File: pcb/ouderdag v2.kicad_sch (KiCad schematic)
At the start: 18 parts, among them J1 Conn_01x05_Pin, J2 Conn_01x05_Pin, J3 Conn_01x05_Socket, J4 Conn_01x05_Socket, J5 Conn_01x06_Pin, SW1 SW_Push, U1 ATtiny85

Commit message: updated code and pcb
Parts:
- removed C1: C, Capacitor_THT:CP_Radial_D8.0mm_P3.50mm, symbol Device:C
- removed J5: Conn_01x06_Pin, Connector_PinHeader_2.54mm:PinHeader_1x06_P2.54mm_Vertical, symbol Connector:Conn_01x06_Pin
- added J5: Conn_01x03_Socket, Connector_PinSocket_2.54mm:PinSocket_1x03_P2.54mm_Vertical, symbol Connector:Conn_01x03_Socket
- added J6: Conn_01x03_Pin, Connector_PinHeader_2.54mm:PinHeader_1x03_P2.54mm_Vertical, symbol Connector:Conn_01x03_Pin
- added SW2: SW-18020P, lib:SW-18020P, symbol rur:SW-18020P
- D1, D2, D3, D4, D5, D6, D7: footprint LED_THT:LED_D8.0mm -> LED_THT:LED_D10.0mm
- J1, J2: value Conn_01x05_Pin -> Conn_01x03_Pin; footprint Connector_PinHeader_2.54mm:PinHeader_1x05_P2.54mm_Vertical -> Connector_PinHeader_2.54mm:PinHeader_1x03_P2.54mm_Vertical; symbol Connector:Conn_01x05_Pin -> Connector:Conn_01x03_Pin
- J3, J4: value Conn_01x05_Socket -> Conn_01x03_Socket; footprint Connector_PinSocket_2.54mm:PinSocket_1x05_P2.54mm_Vertical -> Connector_PinSocket_2.54mm:PinSocket_1x03_P2.54mm_Vertical; symbol Connector:Conn_01x05_Socket -> Connector:Conn_01x03_Socket
- R1, R2: value 220R -> 100R
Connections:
- net GND: now also J5.1 (Pin_1), J5.3 (Pin_3), J6.1 (Pin_1), J6.3 (Pin_3), SW2.1; no longer J1.5 (Pin_5), J2.5 (Pin_5), J3.5 (Pin_5), J4.5 (Pin_5)
- net 1 renamed PB0
- net 2 renamed PB1
- net 3 renamed PB2
- removed net 4: J1.4 (Pin_4), J2.4 (Pin_4), J3.4 (Pin_4), J4.4 (Pin_4), SW1.2, U1.3 (XTAL2/PB4)
- net RST renamed PB5
- new net PB4: J5.2 (Pin_2), J6.2 (Pin_2), SW1.2, SW2.2, U1.3 (XTAL2/PB4)
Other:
- moved on the sheet: BT1, D1, D2, D3, D4, D5, D6, D7, R1, R2, SW1, U1

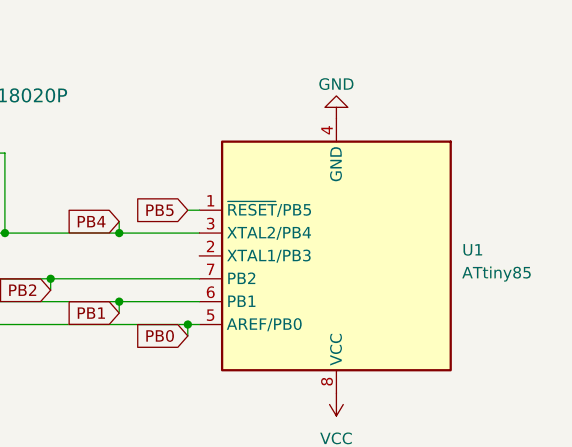
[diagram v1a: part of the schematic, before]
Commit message: change to generic ATtiny
PCB changes:
version 1.0 -> version 1.1
ATtiny85 -> ATtiny
mousebite trace FFF -> FBF
removed order number
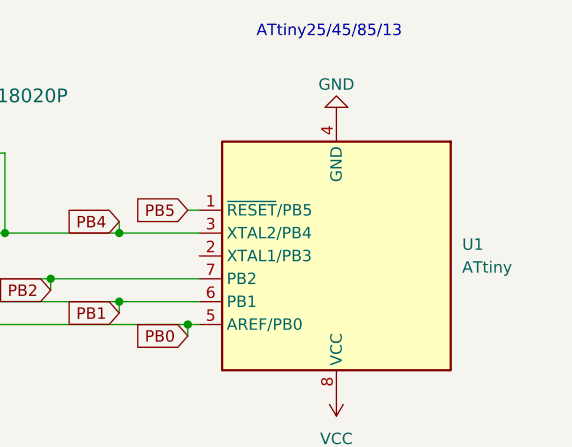
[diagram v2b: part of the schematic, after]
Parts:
- SW1: footprint (none) -> Button_Switch_THT:SW_PUSH-12mm
- U1: value ATtiny85 -> ATtiny
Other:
- note added: "ATtiny25/45/85/13"
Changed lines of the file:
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@@
   (title_block
     (title "Digi Dobbelsteen")
-    (date "2024-01-26")
-    (rev "0.1")
+    (date "2025-03-27")
+    (rev "0.2")
   )
   (junction (at 146.05 66.04) (diameter 0) (color 0 0 0 0)
@@
   (wire (pts (xy 40.64 53.34) (xy 40.64 55.88))
     (stroke (width 0) (type default))
+  )
+  (text "ATtiny25/45/85/13" (at 161.29 36.83 0)
+    (effects (font (size 1.27 1.27)) (justify left bottom))
   )
   (global_label "PB1" (shape input) (at 67.31 107.95 180) (fields_autoplaced)
@@
   (symbol (lib_id "MCU_Microchip_ATtiny:ATtiny45-20P") (at 170.18 60.96 180) (unit 1)
     (in_bom yes) (on_board yes) (dnp no) (fields_autoplaced)
-    (property "Reference" "U1" (at 184.15 60.325 0)
+    (property "Reference" "U1" (at 184.15 59.69 0)
       (effects (font (size 1.27 1.27)) (justify right))
     )
-    (property "Value" "ATtiny85" (at 184.15 62.865 0)
+    (property "Value" "ATtiny" (at 184.15 62.23 0)
       (effects (font (size 1.27 1.27)) (justify right))
     )
@@
       (effects (font (size 1.27 1.27)))
     )
-    (property "Footprint" "" (at 125.73 53.34 0)
-      (effects (font (size 1.27 1.27)) hide)
-    )
+    (property "Footprint" "Button_Switch_THT:SW_PUSH-12mm" (at 125.73 53.34 0)
+      (effects (font (size 1.27 1.27)) hide)
+    )
